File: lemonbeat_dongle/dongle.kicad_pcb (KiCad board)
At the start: 4 copper layers, 50 x 20 mm, 78 parts, among them J201 USB_A, J202 Prog, J203 u.FL, J301 SMA, SW201 SW_Push, U201 nRF52840, U301 Si4467, Y201 32MHz, Y202 32.768kHz, Y301 26MHz

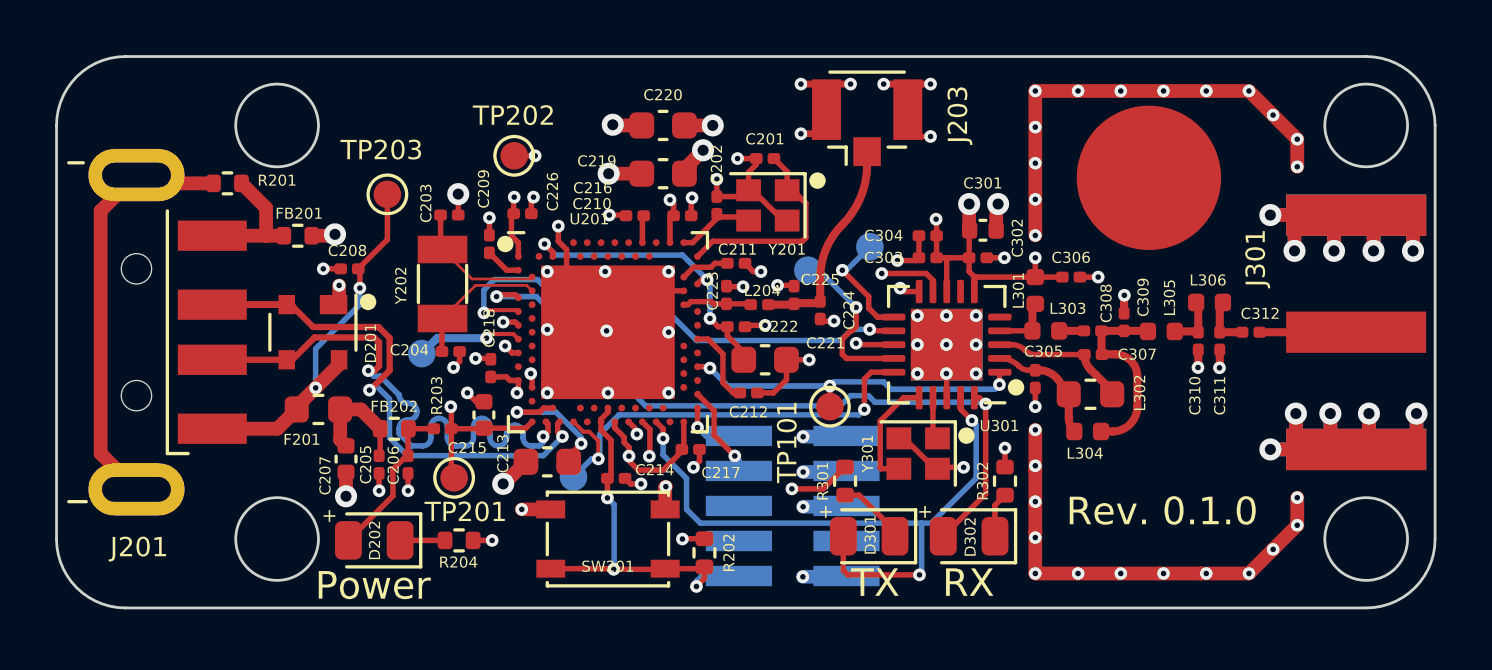
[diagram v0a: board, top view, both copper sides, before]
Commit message: dongle: PCB: move components await from holes
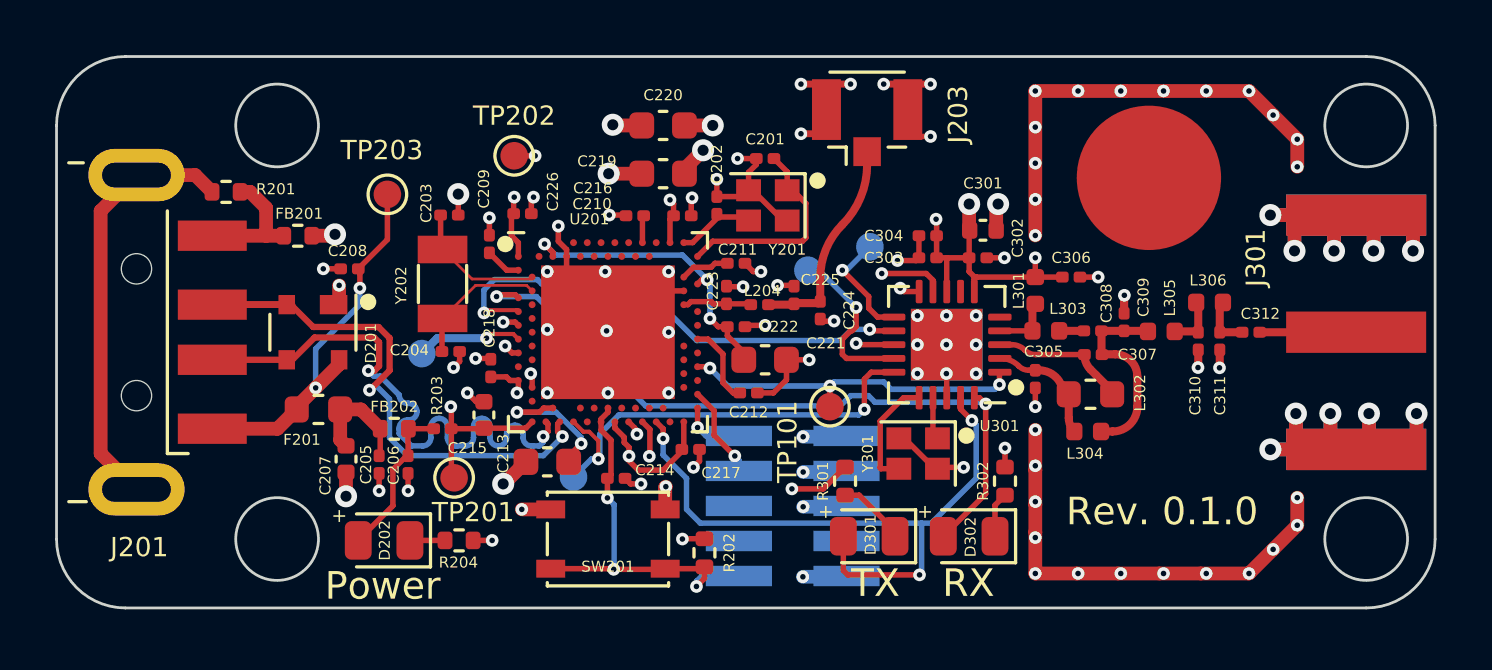
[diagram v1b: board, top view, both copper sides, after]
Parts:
- moved D202 0.35 mm to (122.4, 111.5)
- moved R201 0.31 mm to (116.7, 98.9)
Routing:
- net Net-(J201-Pad5): track 15.0 -> 15.5 mm
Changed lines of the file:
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@@
     (property "Sheetname" "MCU")
     (attr exclude_from_pos_files)
-    (fp_text reference "TP201" (at 0.43 1.245) (layer "F.SilkS")
+    (fp_text reference "TP201" (at 0.69 1.25) (layer "F.SilkS")
       (effects (font (size 0.7 0.7) (thickness 0.15)))
     )
@@
   )
   (footprint "LED_SMD:LED_0805_2012Metric" (layer "F.Cu")
-    (at 122.025 111.55 180)
+    (at 122.38 111.55 180)
     (descr "LED SMD 0805 (2012 Metric), square (rectangular) end terminal, IPC_7351 nominal, (Body size source: https://docs.google.com/spreadsheets/d/1BsfQQcO9C6DZCsRaXUlFlo91Tg2WpOkGARC1WS5S8t0/edit?usp=sharing), generated with kicad-footprint-generator")
     (tags "LED")
@@
   )
   (footprint "Resistor_SMD:R_0402_1005Metric" (layer "F.Cu")
-    (at 116.7 98.6)
+    (at 116.65 98.91)
     (descr "Resistor SMD 0402 (1005 Metric), square (rectangular) end terminal, IPC_7351 nominal, (Body size source: IPC-SM-782 page 72, https://www.pcb-3d.com/wordpress/wp-content/uploads/ipc-sm-782a_amendment_1_and_2.pdf), generated with kicad-footprint-generator")
     (tags "resistor")
@@
   (gr_arc (start 160.5 111.5) (mid 159.767767 113.267767) (end 158 114) (layer "Edge.Cuts") (width 0.1))
   (gr_line (start 113 94) (end 158 94) (layer "Edge.Cuts") (width 0.1))
-  (gr_text "Power" (at 121.975 113.2) (layer "F.SilkS")
+  (gr_text "Power" (at 122.33 113.2) (layer "F.SilkS")
     (effects (font (size 1 1) (thickness 0.15)))
   )
-  (gr_text "+" (at 120.4 110.65) (layer "F.SilkS")
+  (gr_text "+" (at 120.755 110.65) (layer "F.SilkS")
     (effects (font (size 0.5 0.5) (thickness 0.1)))
   )
@@
   (segment (start 120.7875 106.8) (end 120.7875 107.9075) (width 0.5) (layer "F.Cu") (net 6))
   (segment (start 123.25 107.51) (end 123.26 107.5) (width 0.2) (layer "F.Cu") (net 7))
-  (segment (start 122.7 108.977552) (end 122.7 109.9375) (width 0.2) (layer "F.Cu") (net 7))
-  (segment (start 123.197552 108.48) (end 122.7 108.977552) (width 0.2) (layer "F.Cu") (net 7))
+  (segment (start 122.7 108.977552) (end 122.7 110.2925) (width 0.2) (layer "F.Cu") (net 7))
+  (segment (start 122.7 110.2925) (end 121.4425 111.55) (width 0.2) (layer "F.Cu") (net 7))
   (segment (start 123.26 107.5) (end 124.18 107.5) (width 0.2) (layer "F.Cu") (net 7))
-  (segment (start 122.7 109.9375) (end 121.0875 111.55) (width 0.2) (layer "F.Cu") (net 7))
   (segment (start 123.25 108.48) (end 123.25 107.51) (width 0.2) (layer "F.Cu") (net 7))
+  (segment (start 123.197552 108.48) (end 122.7 108.977552) (width 0.2) (layer "F.Cu") (net 7))
   (segment (start 122.5 100.64) (end 122.5 99) (width 0.2) (layer "F.Cu") (net 8))
   (segment (start 119.2125 106.8) (end 119.2125 106.704908) (width 0.5) (layer "F.Cu") (net 8))
@@
   (segment (start 122.094359 105.943545) (end 122.006455 105.943545) (width 0.2) (layer "B.Cu") (net 28))
   (segment (start 116.35 100.5) (end 118.1 100.5) (width 0.5) (layer "F.Cu") (net 29))
-  (segment (start 118.1 99.49) (end 117.21 98.6) (width 0.5) (layer "F.Cu") (net 29))
+  (segment (start 117.52 98.91) (end 117.16 98.91) (width 0.5) (layer "F.Cu") (net 29))
+  (segment (start 118.1 99.49) (end 117.52 98.91) (width 0.5) (layer "F.Cu") (net 29))
   (segment (start 118.1 100.5) (end 118.1 99.49) (width 0.5) (layer "F.Cu") (net 29))
   (segment (start 118.1 100.5) (end 118.74 100.5) (width 0.5) (layer "F.Cu") (net 29))
   (segment (start 112.1 99.6) (end 113.4 98.3) (width 0.5) (layer "F.Cu") (net 30))
   (segment (start 113.4 109.7) (end 112.1 108.4) (width 0.5) (layer "F.Cu") (net 30))
+  (segment (start 115.53 98.3) (end 116.14 98.91) (width 0.5) (layer "F.Cu") (net 30))
   (segment (start 112.1 108.4) (end 112.1 99.6) (width 0.5) (layer "F.Cu") (net 30))
-  (segment (start 116.19 98.6) (end 113.7 98.6) (width 0.5) (layer "F.Cu") (net 30))
+  (segment (start 113.4 98.3) (end 115.53 98.3) (width 0.5) (layer "F.Cu") (net 30))
   (segment (start 133.75 107.4565) (end 133.75 106.75) (width 0.2) (layer "F.Cu") (net 31))
   (via (at 133.75 107.4565) (size 0.46) (drill 0.2) (layers "F.Cu" "B.Cu") (net 31))
@@
   (segment (start 140.777 104.231744) (end 139.824744 105.184) (width 0.2) (layer "In2.Cu") (net 39))
   (segment (start 138.852256 104.861) (end 138.639 104.861) (width 0.2) (layer "In2.Cu") (net 39))
-  (segment (start 124.59 111.55) (end 122.9625 111.55) (width 0.2) (layer "F.Cu") (net 40))
+  (segment (start 123.3175 111.55) (end 124.59 111.55) (width 0.2) (layer "F.Cu") (net 40))
   (segment (start 140.9125 111.4) (end 140.9125 111.2125) (width 0.2) (layer "F.Cu") (net 41))
   (segment (start 139.61 109.91) (end 139.1 109.91) (width 0.2) (layer "F.Cu") (net 41))

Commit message: dongle: PCB: move all test points to bottom side
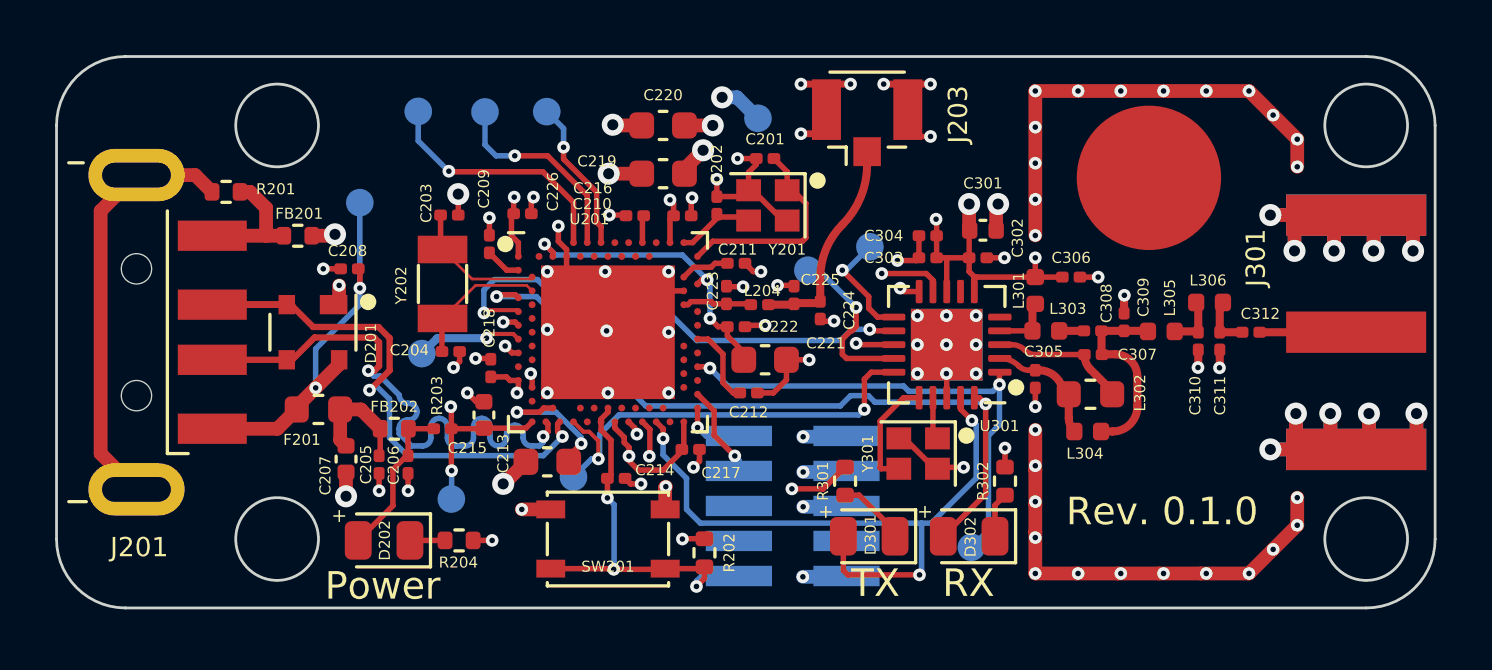
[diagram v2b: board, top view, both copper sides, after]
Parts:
- added TP204: TestPoint, TestPoint:TestPoint_Pad_D1.0mm, B.Cu at (128.3, 96.0)
- added TP205: TestPoint, TestPoint:TestPoint_Pad_D1.0mm, B.Cu at (126.0, 96.0)
- added TP206: TestPoint, TestPoint:TestPoint_Pad_D1.0mm, B.Cu at (123.6, 96.0)
- TP101, TP201, TP202, TP203: moved to B.Cu
- moved TP202 8.94 mm to (135.9, 96.2), turned to 180 degrees
- moved TP101 7.23 mm to (143.7, 111.8), turned to 180 degrees
- moved TP203 1.04 mm to (121.5, 99.3), turned to 180 degrees
- moved TP201 0.78 mm to (124.8, 110.0), turned to 180 degrees
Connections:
- U201 pad A10: unconnected-(U201-PadA10) -> Net-(TP205-Pad1)
- U201 pad A12: unconnected-(U201-PadA12) -> Net-(TP204-Pad1)
- U201 pad A8: unconnected-(U201-PadA8) -> Net-(TP206-Pad1)
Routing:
- net Net-(TP206-Pad1): track 0.00 -> 9.08 mm, vias 0 -> 1
- net Net-(TP205-Pad1): track 0.00 -> 7.37 mm, vias 0 -> 1
- net Net-(TP204-Pad1): track 0.00 -> 5.57 mm, vias 0 -> 1
- net /MCU/P1.04: track 12.7 -> 18.2 mm, vias 3 -> 2
- net VDD: track 27.0 -> 27.8 mm
- net /MCU/VBUS_nRF: track 9.58 -> 10.3 mm, vias 2 -> 3

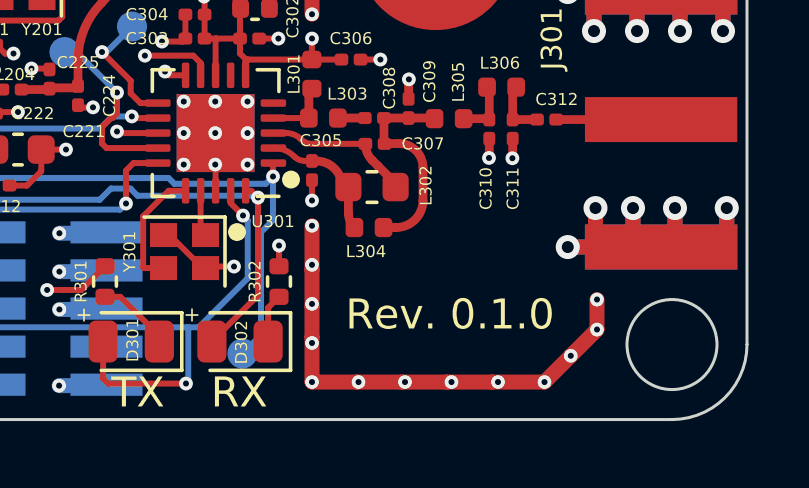
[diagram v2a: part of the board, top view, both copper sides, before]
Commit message: dongle: increase version number to 0.2.0
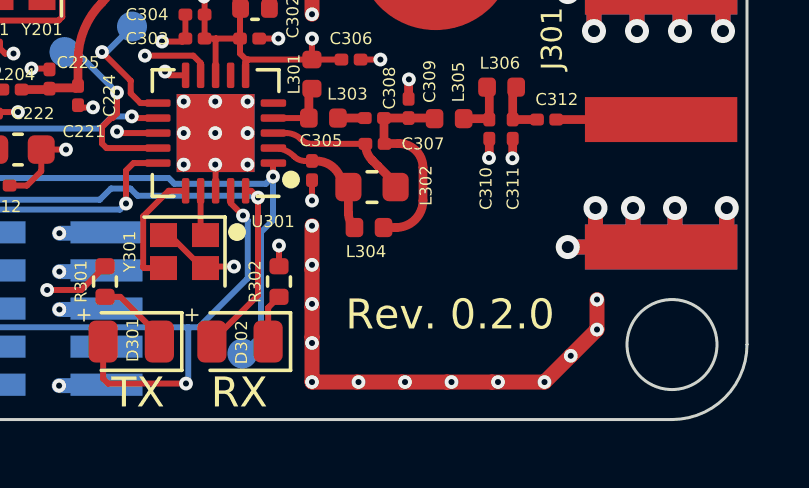
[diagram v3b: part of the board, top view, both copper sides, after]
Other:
- board text added: "Rev. 0.2.0"
- board text removed: "Rev. 0.1.0"
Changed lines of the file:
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@@
     (effects (font (size 0.5 0.5) (thickness 0.1)))
   )
-  (gr_text "Rev. 0.1.0" (at 150.6 110.5) (layer "F.SilkS")
+  (gr_text "Rev. 0.2.0" (at 150.6 110.5) (layer "F.SilkS")
     (effects (font (size 1 1) (thickness 0.15)))
   )
